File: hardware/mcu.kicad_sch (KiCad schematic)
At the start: 17 parts, among them J1 Conn_01x04_Pin, J2 Conn_01x03_Pin, SW1 Reset, U8 AMS1117-3.3, U9 STM32F103C8Tx, Y2 8Mhz

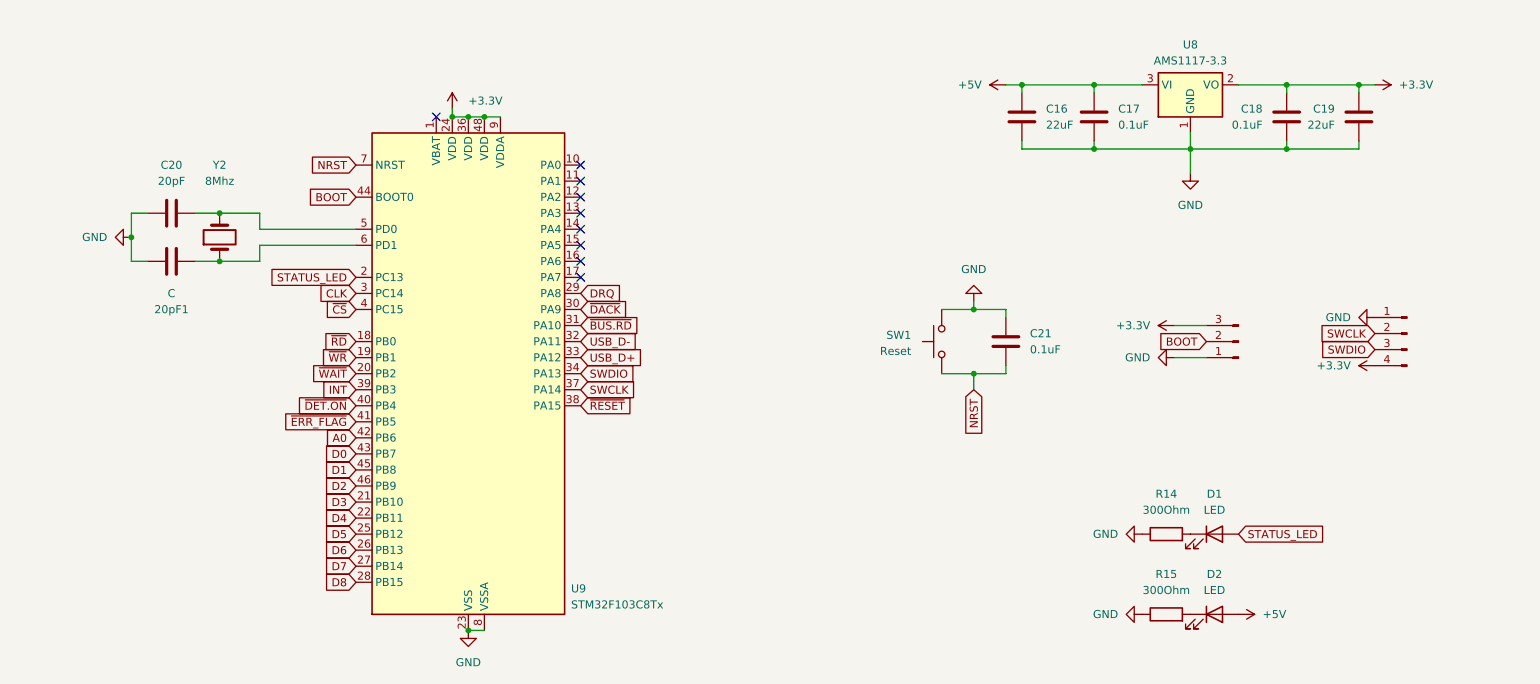
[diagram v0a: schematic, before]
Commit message: hardware: add more capacitors, fix critical mistakes in schematic
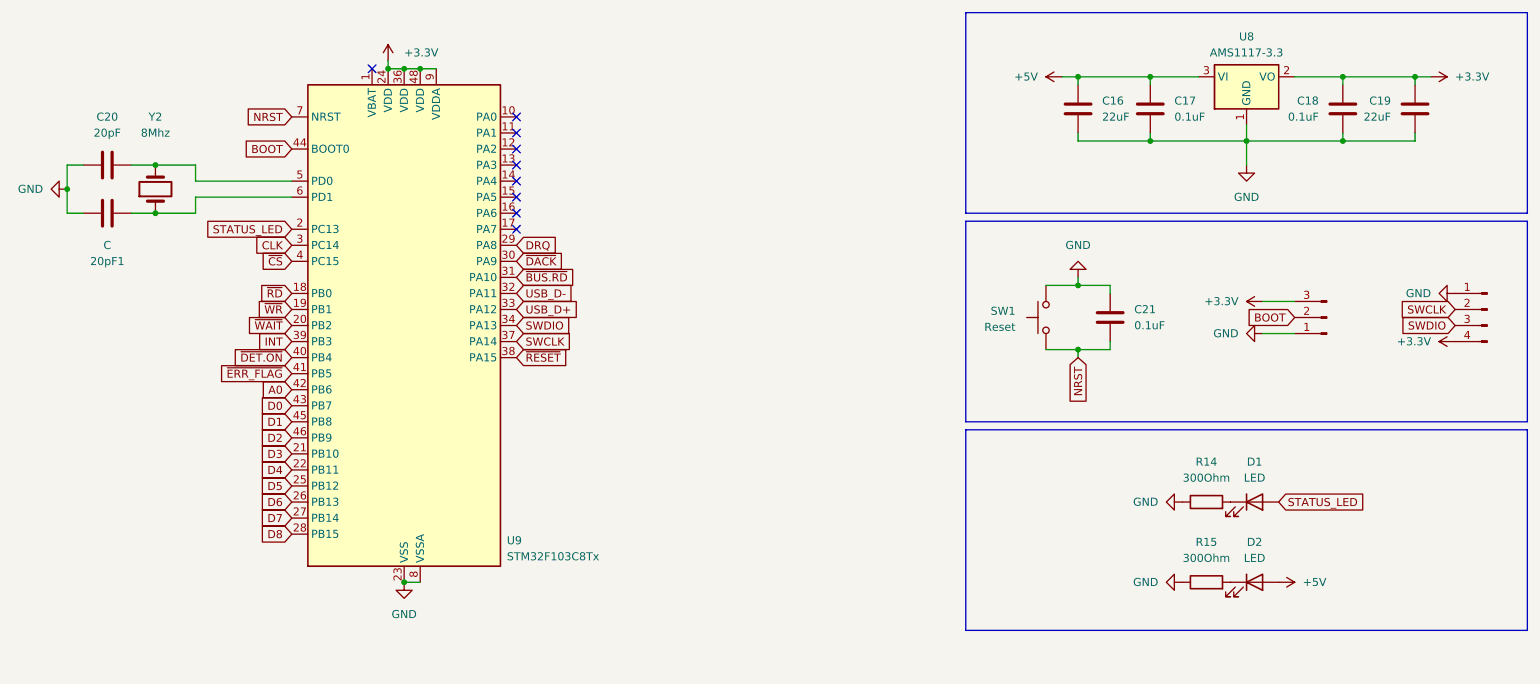
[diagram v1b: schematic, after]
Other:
- moved on the sheet: 20pF1, C16, C17, C18, C19, C20, C21, D1, D2, R14, R15, SW1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

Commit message: hardware: connect MBM module like Compass
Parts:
- removed D2: LED, LED_SMD:LED_0805_2012Metric_Pad1.15x1.40mm_HandSolder, symbol Device:LED
- removed R15: 300Ohm, Resistor_SMD:R_0805_2012Metric_Pad1.20x1.40mm_HandSolder, symbol Device:R
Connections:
- net ~{RESET.MCU}: now reaches U9.17 (PA7)
- net ~{RESET} renamed ~{RESET.BUS}
- no-connect marks 9 -> 8

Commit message: hardware: add powerfail circuit, rework power
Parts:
- renumbered C20 to C29, C16 to C30, C21 to C31, C17 to C32, C18 to C33, C19 to C34, D1 to D4, J2 to J1, J1 to J2, U9 to U10, U8 to U11
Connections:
- net ~{RESET.MCU}: no longer names the net of U10.17 (PA7)
- no-connect marks 8 -> 9
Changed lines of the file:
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@@
 	)
 	(no_connect
+		(at 113.03 81.28)
+	)
+	(no_connect
 		(at 113.03 66.04)
 	)
@@
 		)
 	)
-	(global_label "~{RESET.MCU}"
-		(shape input)
-		(at 113.03 81.28 0)
-		(fields_autoplaced yes)
-		(effects
-			(font
-				(size 1.27 1.27)
-			)
-			(justify left)
-		)
-		(property "Intersheetrefs" "${INTERSHEET_REFS}"
-			(at 126.417 81.28 0)
-			(hide yes)
-			(show_name no)
-			(do_not_autoplace no)
-			(effects
-				(font
-					(size 1.27 1.27)
-				)
-				(justify left)
-			)
-		)
-	)
 	(global_label "D8"
 		(shape input)
@@
 		(dnp no)
 		(fields_autoplaced yes)
-		(property "Reference" "#PWR040"
+		(property "Reference" "#PWR055"
 			(at 254 57.15 0)
 			(hide yes)
@@
 			(project "bubble"
 				(path "/5a4ee61a-7946-4e5f-a476-7e1dac207e84"
-					(reference "#PWR040")
+					(reference "#PWR055")
 					(unit 1)
 				)
@@
 		(dnp no)
 		(fields_autoplaced yes)
-		(property "Reference" "#PWR052"
+		(property "Reference" "#PWR048"
 			(at 95.25 143.51 0)
 			(hide yes)
@@
 			(project "bubble"
 				(path "/5a4ee61a-7946-4e5f-a476-7e1dac207e84"
-					(reference "#PWR052")
+					(reference "#PWR048")
 					(unit 1)
 				)
@@
 		(dnp no)
 		(fields_autoplaced yes)
-		(property "Reference" "#PWR045"
+		(property "Reference" "#PWR056"
 			(at 255.27 91.44 0)
 			(hide yes)
@@
 			(project "bubble"
 				(path "/5a4ee61a-7946-4e5f-a476-7e1dac207e84"
-					(reference "#PWR045")
+					(reference "#PWR056")
 					(unit 1)
 				)
@@
 		(dnp no)
 		(fields_autoplaced yes)
-		(property "Reference" "#PWR046"
+		(property "Reference" "#PWR053"
 			(at 234.95 92.71 0)
 			(hide yes)
@@
 			(project "bubble"
 				(path "/5a4ee61a-7946-4e5f-a476-7e1dac207e84"
-					(reference "#PWR046")
+					(reference "#PWR053")
 					(unit 1)
 				)
@@
 		(dnp no)
 		(fields_autoplaced yes)
-		(property "Reference" "#PWR039"
+		(property "Reference" "#PWR049"
 			(at 203.2 57.15 0)
 			(hide yes)
@@
 			(project "bubble"
 				(path "/5a4ee61a-7946-4e5f-a476-7e1dac207e84"
-					(reference "#PWR039")
+					(reference "#PWR049")
 					(unit 1)
 				)
@@
 		(dnp no)
 		(fields_autoplaced yes)
-		(property "Reference" "#PWR047"
+		(property "Reference" "#PWR054"
 			(at 224.79 97.79 0)
 			(hide yes)
@@
 			(project "bubble"
 				(path "/5a4ee61a-7946-4e5f-a476-7e1dac207e84"
-					(reference "#PWR047")
+					(reference "#PWR054")
 					(unit 1)
 				)
@@
 		(in_pos_files yes)
 		(dnp no)
-		(property "Reference" "C18"
+		(property "Reference" "C33"
 			(at 240.03 60.9599 0)
 			(show_name no)
@@
 			(project "bubble"
 				(path "/5a4ee61a-7946-4e5f-a476-7e1dac207e84"
-					(reference "C18")
+					(reference "C33")
 					(unit 1)
 				)
@@
 		(in_pos_files yes)
 		(dnp no)
-		(property "Reference" "J1"
+		(property "Reference" "J2"
 			(at 266.065 86.36 0)
 			(hide yes)
@@
 			(project "bubble"
 				(path "/5a4ee61a-7946-4e5f-a476-7e1dac207e84"
-					(reference "J1")
+					(reference "J2")
 					(unit 1)
 				)
@@
 		(in_pos_files yes)
 		(dnp no)
-		(property "Reference" "D1"
+		(property "Reference" "D4"
 			(at 229.87 118.11 0)
 			(show_name no)
@@
 			(project "bubble"
 				(path "/5a4ee61a-7946-4e5f-a476-7e1dac207e84"
-					(reference "D1")
+					(reference "D4")
 					(unit 1)
 				)
@@
 		(dnp no)
 		(fields_autoplaced yes)
-		(property "Reference" "#PWR049"
+		(property "Reference" "#PWR051"
 			(at 212.09 124.46 0)
 			(hide yes)
@@
 			(project "bubble"
 				(path "/5a4ee61a-7946-4e5f-a476-7e1dac207e84"
-					(reference "#PWR049")
+					(reference "#PWR051")
 					(unit 1)
 				)
@@
 		(dnp no)
 		(fields_autoplaced yes)
-		(property "Reference" "C16"
+		(property "Reference" "C30"
 			(at 205.74 60.9599 0)
 			(show_name no)
@@
 			(project "bubble"
 				(path "/5a4ee61a-7946-4e5f-a476-7e1dac207e84"
-					(reference "C16")
+					(reference "C30")
 					(unit 1)
 				)
@@
 		(dnp no)
 		(fields_autoplaced yes)
-		(property "Reference" "#PWR043"
+		(property "Reference" "#PWR046"
 			(at 35.56 74.93 0)
 			(hide yes)
@@
 			(project "bubble"
 				(path "/5a4ee61a-7946-4e5f-a476-7e1dac207e84"
-					(reference "#PWR043")
+					(reference "#PWR046")
 					(unit 1)
 				)
@@
 		(dnp no)
 		(fields_autoplaced yes)
-		(property "Reference" "#PWR044"
+		(property "Reference" "#PWR050"
 			(at 201.93 82.55 0)
 			(hide yes)
@@
 			(project "bubble"
 				(path "/5a4ee61a-7946-4e5f-a476-7e1dac207e84"
-					(reference "#PWR044")
+					(reference "#PWR050")
 					(unit 1)
 				)
@@
 		(dnp no)
 		(fields_autoplaced yes)
-		(property "Reference" "C17"
+		(property "Reference" "C32"
 			(at 217.17 60.9599 0)
 			(show_name no)
@@
 			(project "bubble"
 				(path "/5a4ee61a-7946-4e5f-a476-7e1dac207e84"
-					(reference "C17")
+					(reference "C32")
 					(unit 1)
 				)
@@
 		(dnp no)
 		(fields_autoplaced yes)
-		(property "Reference" "#PWR048"
+		(property "Reference" "#PWR057"
 			(at 265.43 99.06 0)
 			(hide yes)
@@
 			(project "bubble"
 				(path "/5a4ee61a-7946-4e5f-a476-7e1dac207e84"
-					(reference "#PWR048")
+					(reference "#PWR057")
 					(unit 1)
 				)
@@
 		(in_pos_files yes)
 		(dnp no)
-		(property "Reference" "C19"
+		(property "Reference" "C34"
 			(at 251.46 60.9599 0)
 			(show_name no)
@@
 			(project "bubble"
 				(path "/5a4ee61a-7946-4e5f-a476-7e1dac207e84"
-					(reference "C19")
+					(reference "C34")
 					(unit 1)
 				)
@@
 		(dnp no)
 		(fields_autoplaced yes)
-		(property "Reference" "U8"
+		(property "Reference" "U11"
 			(at 228.6 50.8 0)
 			(show_name no)
@@
 			(project "bubble"
 				(path "/5a4ee61a-7946-4e5f-a476-7e1dac207e84"
-					(reference "U8")
+					(reference "U11")
 					(unit 1)
 				)
@@
 		(dnp no)
 		(fields_autoplaced yes)
-		(property "Reference" "#PWR041"
+		(property "Reference" "#PWR047"
 			(at 92.71 58.42 0)
 			(hide yes)
@@
 			(project "bubble"
 				(path "/5a4ee61a-7946-4e5f-a476-7e1dac207e84"
-					(reference "#PWR041")
+					(reference "#PWR047")
 					(unit 1)
 				)
@@
 		(dnp no)
 		(fields_autoplaced yes)
-		(property "Reference" "C20"
+		(property "Reference" "C29"
 			(at 48.26 63.5 90)
 			(show_name no)
@@
 			(project "bubble"
 				(path "/5a4ee61a-7946-4e5f-a476-7e1dac207e84"
-					(reference "C20")
+					(reference "C29")
 					(unit 1)
 				)
@@
 		(in_pos_files yes)
 		(dnp no)
-		(property "Reference" "U9"
+		(property "Reference" "U10"
 			(at 111.506 130.556 0)
 			(show_name no)
@@
 			(project "bubble"
 				(path "/5a4ee61a-7946-4e5f-a476-7e1dac207e84"
-					(reference "U9")
+					(reference "U10")
 					(unit 1)
 				)
@@
 		(dnp no)
 		(fields_autoplaced yes)
-		(property "Reference" "C21"
+		(property "Reference" "C31"
 			(at 210.82 93.9799 0)
 			(show_name no)
@@
 			(project "bubble"
 				(path "/5a4ee61a-7946-4e5f-a476-7e1dac207e84"
-					(reference "C21")
+					(reference "C31")
 					(unit 1)
 				)
@@
 		(dnp no)
 		(fields_autoplaced yes)
-		(property "Reference" "#PWR042"
+		(property "Reference" "#PWR052"
 			(at 228.6 77.47 0)
 			(hide yes)
@@
 			(project "bubble"
 				(path "/5a4ee61a-7946-4e5f-a476-7e1dac207e84"
-					(reference "#PWR042")
+					(reference "#PWR052")
 					(unit 1)
 				)
@@
 		(dnp no)
 		(fields_autoplaced yes)
-		(property "Reference" "J2"
+		(property "Reference" "J1"
 			(at 242.57 93.9799 0)
 			(hide yes)
@@
 			(project "bubble"
 				(path "/5a4ee61a-7946-4e5f-a476-7e1dac207e84"
-					(reference "J2")
+					(reference "J1")
 					(unit 1)
 				)

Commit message: hardware: connect input signals from 7220 to stm32 five tolerant pins
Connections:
- net ~{BUS.RD} is gone; now on net ~{ERR_FLAG}: U10.31 (PA10)
- net A0: now also U10.40 (PB4); no longer U10.42 (PB6)
- net DRQ: now also U10.41 (PB5); no longer U10.29 (PA8)
- net ~{CS}: now also U10.17 (PA7); no longer U10.4 (PC15)
- net ~{DACK}: now also U10.42 (PB6); no longer U10.30 (PA9)
- net ~{DET.ON}: now also U10.30 (PA9); no longer U10.40 (PB4)
- net ~{ERR_FLAG}: no longer U10.41 (PB5)
- net CLK: no longer names the net of U10.3 (PC14)
- net ~{RESET.BUS} renamed MBM CLK
- new net ~{RESET}: U10.29 (PA8)
- no-connect marks 9 -> 10
